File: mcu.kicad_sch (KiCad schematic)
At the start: 4 parts, among them SW1 SW_EN, SW2 SW_IO0, U1 ESP32-C6-MINI-1

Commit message: add uwm and refactoring
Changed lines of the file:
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@@
+	(bus
+		(pts
+			(xy 196.85 106.68) (xy 196.85 114.3)
+		)
+		(stroke
+			(width 0)
+			(type default)
+		)
+	)
 	(bus
 		(pts
@@
 		)
 	)
+	(bus
+		(pts
+			(xy 198.12 105.41) (xy 196.85 106.68)
+		)
+		(stroke
+			(width 0)
+			(type default)
+		)
+	)
 	(wire
 		(pts
@@
 		(pts
 			(xy 154.94 77.47) (xy 156.21 77.47)
+		)
+		(stroke
+			(width 0)
+			(type default)
+		)
+	)
+	(bus
+		(pts
+			(xy 201.93 105.41) (xy 198.12 105.41)
 		)
 		(stroke
@@
 		)
 	)
+	(hierarchical_label "{MISO MOSI CLK}"
+		(shape bidirectional)
+		(at 201.93 105.41 0)
+		(effects
+			(font
+				(size 1.27 1.27)
+			)
+			(justify left)
+		)
+	)

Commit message: improve design
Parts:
- C1: footprint (none) -> Capacitor_SMD:C_0402_1005Metric; LCSC (none) -> C77020
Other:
- title: (none) -> Dropbot
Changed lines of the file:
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@@
 	(generator_version "10.0")
 	(paper "A4")
+	(title_block
+		(title "Dropbot")
+	)
 	(rectangle
 		(start 121.92 133.35)
@@
 			)
 		)
-		(property "Footprint" ""
+		(property "Footprint" "Capacitor_SMD:C_0402_1005Metric"
 			(at 140.6652 45.72 0)
 			(hide yes)
@@
 			(at 139.7 41.91 0)
 			(hide yes)
+			(show_name no)
+			(do_not_autoplace no)
+			(effects
+				(font
+					(size 1.27 1.27)
+				)
+			)
+		)
+		(property "LCSC" "C77020"
+			(at 139.7 41.91 0)
+			(hide yes)

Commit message: change component code part
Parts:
- C1: LCSC C77020 -> C60474
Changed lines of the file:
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@@
 			)
 		)
-		(property "LCSC" "C77020"
+		(property "LCSC" "C60474"
 			(at 139.7 41.91 0)
 			(hide yes)

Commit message: Add LCSC part for esp32
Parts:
- U1: LCSC (none) -> C5736265
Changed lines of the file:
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@@
+			)
+		)
+		(property "LCSC" "C5736265"
+			(at 139.7 95.25 0)
+			(hide yes)
+			(show_name no)
+			(do_not_autoplace no)
+			(effects
+				(font
+					(size 1.27 1.27)
+				)
 			)
 		)

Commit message: progress on routing
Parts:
- removed U1: ESP32-C6-MINI-1, RF_Module:ESP32-C6-MINI-1, symbol RF_Module:ESP32-C6-MINI-1
- added U6: ESP32-C6-WROOM-1-N8, lib_fp:XCVR_ESP32-C6-WROOM-1-N8, symbol ESP32-C6-WROOM-1-N8:ESP32-C6-WROOM-1-N8
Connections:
- net +3V3: now also U6.2 (3V3)
- net EN: now also U6.3 (EN)
- net GND: now also U6.1 (GND), U6.28 (GND), U6.29_1 (GND), U6.29_2 (GND), U6.29_3 (GND), U6.29_4 (GND), U6.29_5 (GND), U6.29_6 (GND), U6.29_7 (GND), U6.29_8 (GND), U6.29_9 (GND)
- net RX0: now also U6.24 (RXD0/GPIO17)
- net TX0: now also U6.25 (TXD0/GPIO16)
- net USB1.D+: now also U6.14 (IO13)
- net USB1.D-: now also U6.13 (IO12)
- net IO0 renamed IO9
- net IO9: now also U6.15 (IO9)
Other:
- moved on the sheet: C1

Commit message: progress on routing
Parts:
- C1: footprint Capacitor_SMD:C_0402_1005Metric -> Capacitor_SMD:C_0805_2012Metric
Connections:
- net AIN1: now also U6.11 (IO10)
- net AIN2: now also U6.10 (IO8)
- net BIN1: now also U6.8 (IO0)
- net BIN2: now also U6.9 (IO1)
- net CLK: now also U6.4 (IO4)
- net MISO: now also U6.5 (IO5)
- net MOSI: now also U6.6 (IO6)
- net UWB_IRQ: now also U6.27 (IO2)
- net UWB_RST: now also U6.23 (IO15)
- net UWB_WUP: now also U6.26 (IO3)
- net UWB_~{CS}: now also U6.7 (IO7)
- net ~{SLEEP}: now also U6.12 (IO11)

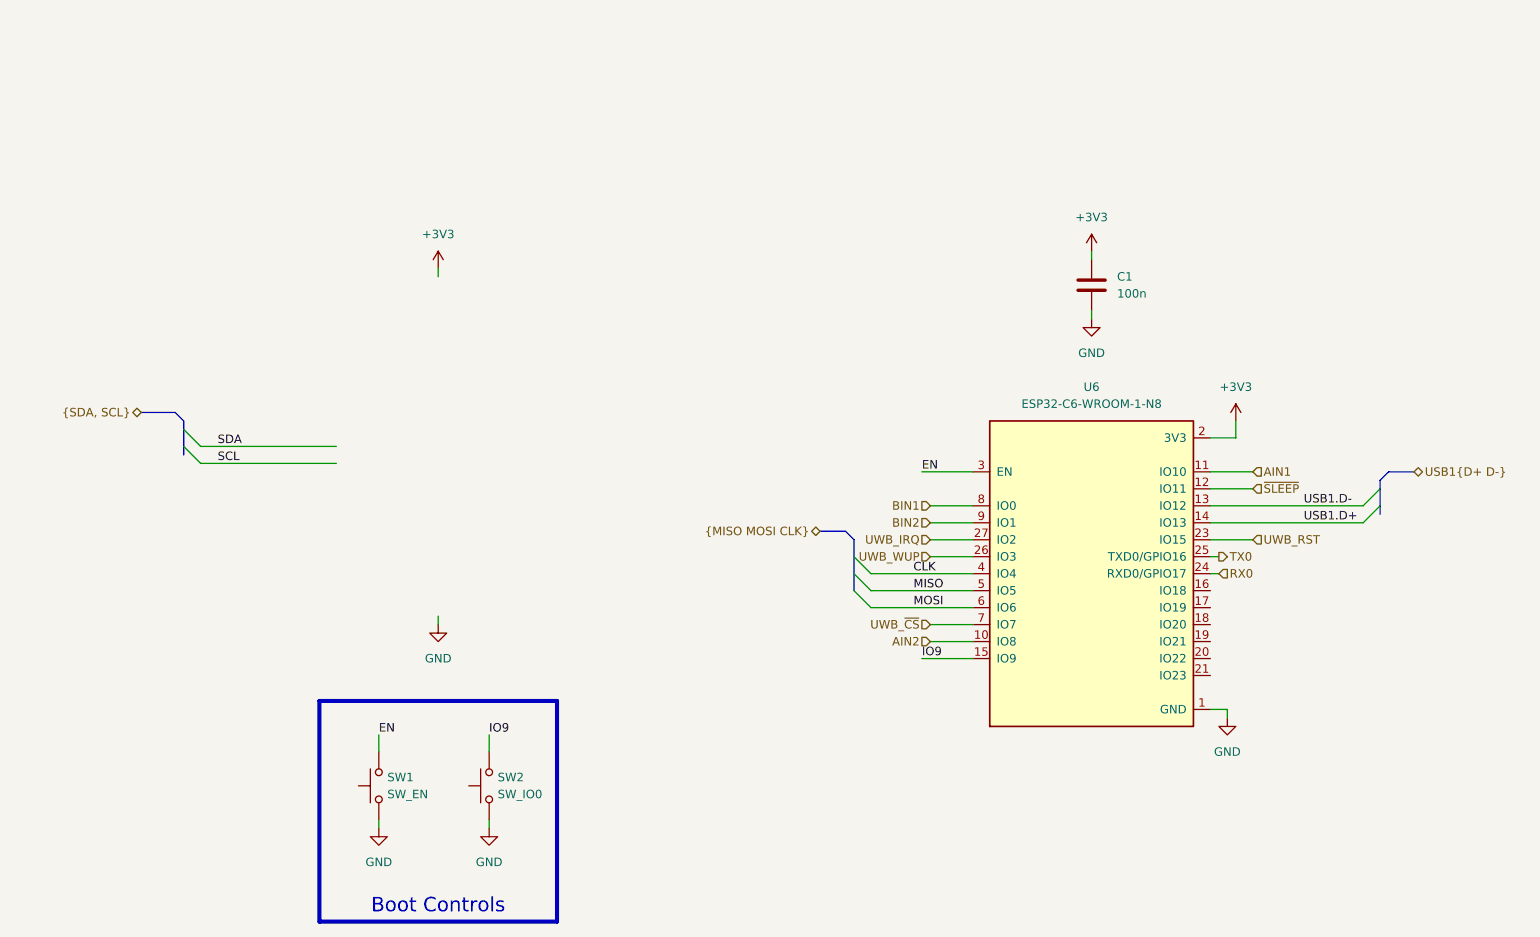
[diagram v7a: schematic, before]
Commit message: consolidated routing
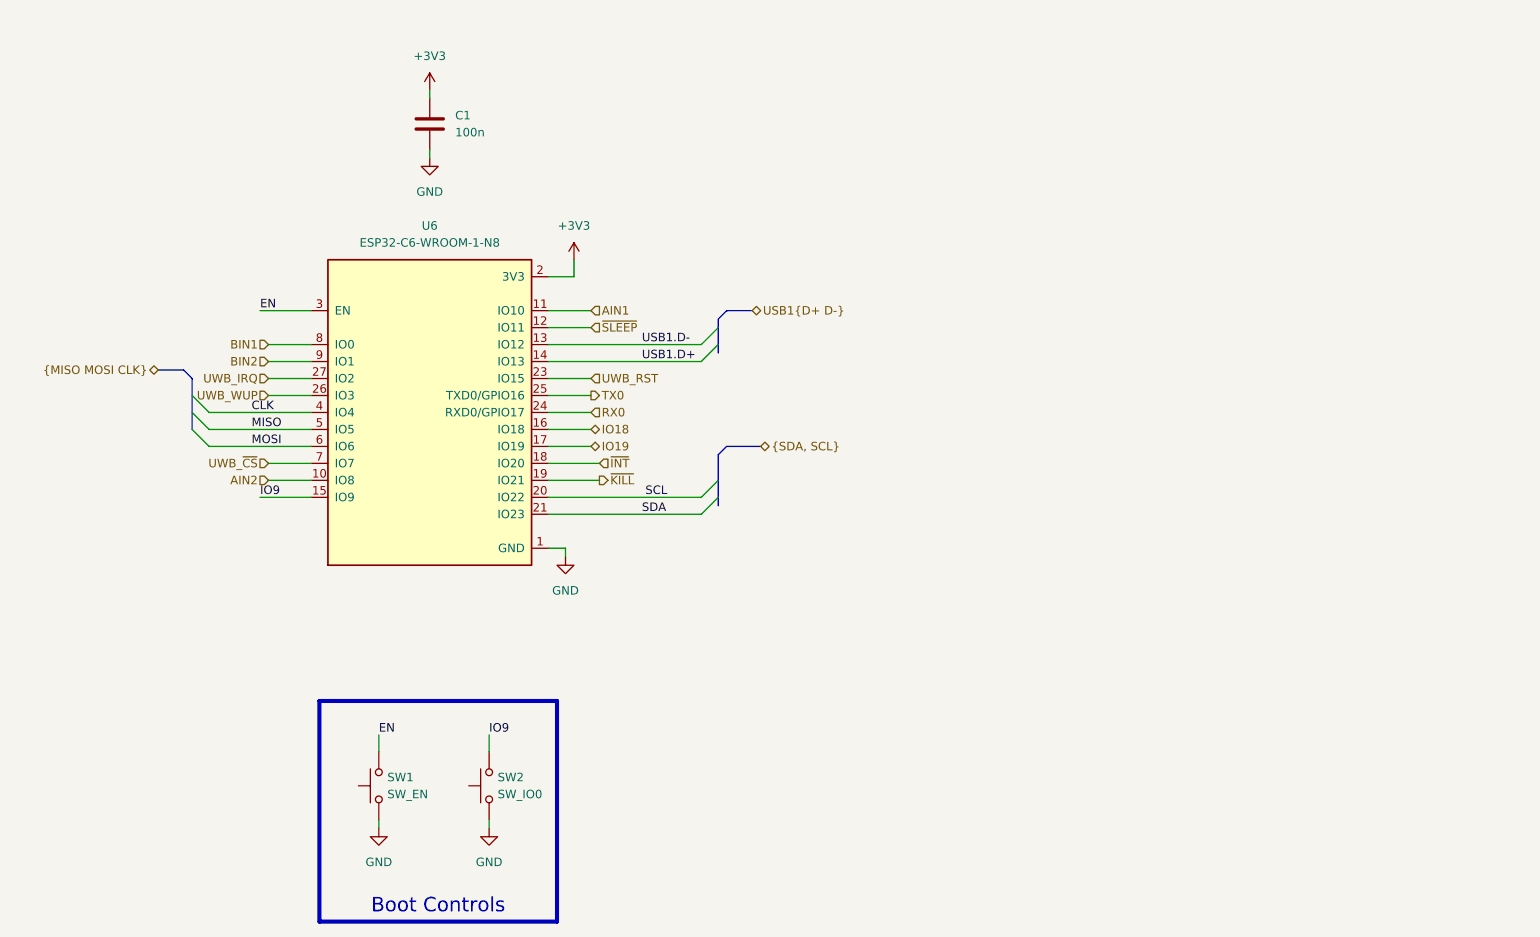
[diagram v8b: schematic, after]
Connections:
- net SCL: now also U6.20 (IO22)
- net SDA: now also U6.21 (IO23)
- net IO18: now reaches U6.16 (IO18)
- net IO19: now reaches U6.17 (IO19)
- net ~{INT}: now reaches U6.18 (IO20)
- net ~{KILL}: now reaches U6.19 (IO21)
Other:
- moved on the sheet: C1, U6
